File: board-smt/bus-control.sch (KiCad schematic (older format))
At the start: 75 parts, among them Q301 Dual_NMOS, Q302 Dual_NMOS, Q303 Dual_NMOS, Q304 Dual_NMOS, Q305 Dual_NMOS, Q306 Dual_NMOS, Q307 Dual_NMOS, U201 CMP401, U204 CMP401, U205 CMP401, U301 CMP401, U302 CMP401, U303 CMP401, U304 CMP401, U305 CMP401

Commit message: Added some voltage regulators.
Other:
- note added: "Need to split the 1.5V reference bus\ninto two halves with separate regulators."
- note removed: "Need to split the 1.5V bus into two\nhalves with separate regulators."
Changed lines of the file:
@@
 	6200 5150 6200 5100
 Text Notes 5350 5900 0    60   ~ 0
-Need to split the 1.5V bus into two\nhalves with separate regulators.
+Need to split the 1.5V reference bus\ninto two halves with separate regulators.
 Wire Wire Line
 	2650 1200 2650 1250

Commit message: Worked on the board layout for the bus receivers.
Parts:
- renumbered Q307 to Q308, U302 to U205, U205 to U302
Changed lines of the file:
@@
 $EndComp
 $Comp
-L CMP401 U205
-U 2 1 58C6BC47
+L CMP401 U302
+U 1 1 58C6BC47
 P 8950 3900
-F 0 "U205" H 9450 4000 60  0000 C CNN
+F 0 "U302" H 9450 4000 60  0000 C CNN
 F 1 "CMP401" H 9550 3700 60  0000 C CNN
 F 2 "Housings_SOIC:SOIC-16_3.9x9.9mm_Pitch1.27mm" H 8950 3900 60  0001 C CNN
 F 3 "" H 8950 3900 60  0001 C CNN
-	2    8950 3900
+	1    8950 3900
 	1    0    0    -1
 $EndComp
@@
 	5450 2150 5350 2150
 $Comp
-L Dual_NMOS Q307
-U 2 1 58C6D401
+L Dual_NMOS Q308
+U 1 1 58C6D401
 P 5500 3200
-F 0 "Q307" H 5450 3100 50  0000 R CNN
+F 0 "Q308" H 5450 3100 50  0000 R CNN
 F 1 "Dual_NMOS" H 5500 3000 50  0000 R CNN
 F 2 "TO_SOT_Packages_SMD:SOT-23-6" H 5700 3300 29  0001 C CNN
 F 3 "" H 5500 3200 60  0000 C CNN
-	2    5500 3200
+	1    5500 3200
 	1    0    0    -1
 $EndComp
@@
 $EndComp
 $Comp
-L CMP401 U302
-U 1 1 58C6D435
+L CMP401 U205
+U 3 1 58C6D435
 P 6000 3150
-F 0 "U302" H 6500 3250 60  0000 C CNN
+F 0 "U205" H 6500 3250 60  0000 C CNN
 F 1 "CMP401" H 6600 2950 60  0000 C CNN
 F 2 "Housings_SOIC:SOIC-16_3.9x9.9mm_Pitch1.27mm" H 6000 3150 60  0001 C CNN
 F 3 "" H 6000 3150 60  0001 C CNN
-	1    6000 3150
+	3    6000 3150
 	1    0    0    -1
 $EndComp
@@
 $Comp
 L CMP401 U205
-U 3 1 58C6FE61
+U 2 1 58C6FE61
 P 1950 2700
 F 0 "U205" H 2450 2800 60  0000 C CNN
@@
 F 2 "Housings_SOIC:SOIC-16_3.9x9.9mm_Pitch1.27mm" H 1950 2700 60  0001 C CNN
 F 3 "" H 1950 2700 60  0001 C CNN
-	3    1950 2700
-	1    0    0    -1
-$EndComp
+	2    1950 2700
+	1    0    0    -1
+$EndComp

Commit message: Moved comparator power connections to separate symbols.
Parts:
- removed R360: 5kΩ, Resistors_SMD:R_0603, symbol R
- R335, R336: value R -> 20kΩ
- R347, R348: value R -> 340kΩ
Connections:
- net labels added: +1V5_ref
- net labels removed: +3V3
- wire segments 231 -> 213
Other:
- note added: "If split the 1.5V reference,\nuse two 10k resistors."
- note removed: "Need to split the 1.5V reference bus\ninto two halves with separate regulators."

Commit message: Little fixups
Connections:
- wire segments 213 -> 156

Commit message: Updated to KiCad v5
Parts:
- Q301, Q302, Q303, Q304, Q305, Q306, Q307, Q308: symbol Dual_NMOS -> myLib:Dual_NMOS
- R301, R302, R303, R304, R305, R306, R307, R308, R309, R310, R311, R312, R313, R314, R315, R316, R317, R318, R319, R320, R321, R322, R323, R324, R325, R326, R327, R328, R329, R330, R331, R332, R333, R334, R335, R336, R337, R338, R339, R340, R341, R342, R343, R344, R345, R346, R347, R348, R349, R350, R351, R352, R353, R354, R355, R356, R357, R358, R359: symbol R -> device:R
- U201, U204, U205, U301, U302, U303, U304, U305: symbol CMP401 -> myLib:CMP401
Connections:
- wire segments 156 -> 212

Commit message: Updated to KiCad v5
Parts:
- R301, R302, R303, R304, R305, R306, R307, R308, R309, R310, R311, R312, R313, R314, R315, R316, R317, R318, R319, R320, R321, R322, R323, R324, R325, R326, R327, R328, R329, R330, R331, R332, R333, R334, R335, R336, R337, R338, R339, R340, R341, R342, R343, R344, R345, R346, R347, R348, R349, R350, R351, R352, R353, R354, R355, R356, R357, R358, R359: symbol device:R -> qsic-rescue:R-device
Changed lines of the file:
@@
 EESchema Schematic File Version 4
 LIBS:qsic-cache
-EELAYER 26 0
+EELAYER 30 0
 EELAYER END
 $Descr A 11000 8500
 encoding utf-8
-Sheet 2 6
+Sheet 2 7
 Title "Bus Control Transceivers"
 Date "2017-10-31"
@@
 $EndComp
 $Comp
-L device:R R323
+L qsic-rescue:R-device R323
 U 1 1 5885877B
 P 8050 1100
@@
 $EndComp
 $Comp
-L device:R R335
+L qsic-rescue:R-device R335
 U 1 1 58858792
 P 8900 1350
@@
 $EndComp
 $Comp
-L device:R R347
+L qsic-rescue:R-device R347
 U 1 1 58858799
 P 9100 1200
@@
 $EndComp
 $Comp
-L device:R R317
+L qsic-rescue:R-device R317
 U 1 1 58859CC4
 P 3650 5500
@@
 $EndComp
 $Comp
-L device:R R318
+L qsic-rescue:R-device R318
 U 1 1 58859CD5
 P 3650 6950
@@
 $EndComp
 $Comp
-L device:R R302
+L qsic-rescue:R-device R302
 U 1 1 58859D09
 P 1500 5300
@@
 $EndComp
 $Comp
-L device:R R301
+L qsic-rescue:R-device R301
 U 1 1 58859D11
 P 1500 4900
@@
 $EndComp
 $Comp
-L device:R R319
+L qsic-rescue:R-device R319
 U 1 1 58859D26
 P 4300 5100
@@
 $EndComp
 $Comp
-L device:R R320
+L qsic-rescue:R-device R320
 U 1 1 58859D2D
 P 4300 5500
@@
 $EndComp
 $Comp
-L device:R R304
+L qsic-rescue:R-device R304
 U 1 1 58859D48
 P 1500 6750
@@
 $EndComp
 $Comp
-L device:R R303
+L qsic-rescue:R-device R303
 U 1 1 58859D55
 P 1500 6350
@@
 $EndComp
 $Comp
-L device:R R321
+L qsic-rescue:R-device R321
 U 1 1 58859D5E
 P 4300 6550
@@
 $EndComp
 $Comp
-L device:R R322
+L qsic-rescue:R-device R322
 U 1 1 58859D6B
 P 4300 6950
@@
 $EndComp
 $Comp
-L device:R R305
+L qsic-rescue:R-device R305
 U 1 1 58859DCE
 P 1500 1000
@@
 $EndComp
 $Comp
-L device:R R311
+L qsic-rescue:R-device R311
 U 1 1 58859DD5
 P 2050 1000
@@
 $EndComp
 $Comp
-L device:R R306
+L qsic-rescue:R-device R306
 U 1 1 58859DF7
 P 1550 1750
@@
 $EndComp
 $Comp
-L device:R R312
+L qsic-rescue:R-device R312
 U 1 1 58859E7E
 P 2100 1750
@@
 	1650 2050 1750 2050
 $Comp
-L device:R R359
+L qsic-rescue:R-device R359
 U 1 1 58865DB5
 P 5900 5300
@@
 $EndComp
 $Comp
-L device:R R324
+L qsic-rescue:R-device R324
 U 1 1 58C69285
 P 8050 1800
@@
 $EndComp
 $Comp
-L device:R R336
+L qsic-rescue:R-device R336
 U 1 1 58C69298
 P 8900 2050
@@
 $EndComp
 $Comp
-L device:R R348
+L qsic-rescue:R-device R348
 U 1 1 58C6929F
 P 9100 1900
@@
 $EndComp
 $Comp
-L device:R R325
+L qsic-rescue:R-device R325
 U 1 1 58C6B57E
 P 8050 2550
@@
 $EndComp
 $Comp
-L device:R R337
+L qsic-rescue:R-device R337
 U 1 1 58C6B591
 P 8900 2800
@@
 $EndComp
 $Comp
-L device:R R349
+L qsic-rescue:R-device R349
 U 1 1 58C6B598
 P 9100 2650
@@
 $EndComp
 $Comp
-L device:R R326
+L qsic-rescue:R-device R326
 U 1 1 58C6B9FE
 P 8050 3250
@@
 $EndComp
 $Comp
-L device:R R338
+L qsic-rescue:R-device R338
 U 1 1 58C6BA11
 P 8900 3500
@@
 $EndComp
 $Comp
-L device:R R350
+L qsic-rescue:R-device R350
 U 1 1 58C6BA18
 P 9100 3350
@@
 $EndComp
 $Comp
-L device:R R327
+L qsic-rescue:R-device R327
 U 1 1 58C6BC1A
 P 8050 3950
@@
 $EndComp
 $Comp
-L device:R R339
+L qsic-rescue:R-device R339
 U 1 1 58C6BC2D
 P 8900 4200
@@
 $EndComp
 $Comp
-L device:R R351
+L qsic-rescue:R-device R351
 U 1 1 58C6BC34
 P 9100 4050
@@
 $EndComp
 $Comp
-L device:R R328
+L qsic-rescue:R-device R328
 U 1 1 58C6C09D
 P 8050 4650
@@
 $EndComp
 $Comp
-L device:R R340
+L qsic-rescue:R-device R340
 U 1 1 58C6C0B0
 P 8900 4900
@@
 $EndComp
 $Comp
-L device:R R352
+L qsic-rescue:R-device R352
 U 1 1 58C6C0B7
 P 9100 4750
@@
 $EndComp
 $Comp
-L device:R R329
+L qsic-rescue:R-device R329
 U 1 1 58C6C381
 P 8050 5350
@@
 $EndComp
 $Comp
-L device:R R341
+L qsic-rescue:R-device R341
 U 1 1 58C6C394
 P 8900 5600
@@
 $EndComp
 $Comp
-L device:R R353
+L qsic-rescue:R-device R353
 U 1 1 58C6C39B
 P 9100 5450
@@
 $EndComp
 $Comp
-L device:R R330
+L qsic-rescue:R-device R330
 U 1 1 58C6C90E
 P 8050 6050
@@
 $EndComp
 $Comp
-L device:R R342
+L qsic-rescue:R-device R342
 U 1 1 58C6C921
 P 8900 6300
@@
 $EndComp
 $Comp
-L device:R R354
+L qsic-rescue:R-device R354
 U 1 1 58C6C928
 P 9100 6150
@@
 $EndComp
 $Comp
-L device:R R331
+L qsic-rescue:R-device R331
 U 1 1 58C6CADA
 P 4600 1200
@@
 $EndComp
 $Comp
-L device:R R343
+L qsic-rescue:R-device R343
 U 1 1 58C6CAED
 P 5450 1450
@@
 $EndComp
 $Comp
-L device:R R355
+L qsic-rescue:R-device R355
 U 1 1 58C6CAF4
 P 5650 1300
@@
 $EndComp
 $Comp
-L device:R R332
+L qsic-rescue:R-device R332
 U 1 1 58C6CDF5
 P 4600 1900
@@
 $EndComp
 $Comp
-L device:R R344
+L qsic-rescue:R-device R344
 U 1 1 58C6CE08
 P 5450 2150
@@
 $EndComp
 $Comp
-L device:R R356
+L qsic-rescue:R-device R356
 U 1 1 58C6CE0F
 P 5650 2000
@@
 $EndComp
 $Comp
-L device:R R333
+L qsic-rescue:R-device R333
 U 1 1 58C6D0CF
 P 4600 2650
@@
 $EndComp
 $Comp
-L device:R R345
+L qsic-rescue:R-device R345
 U 1 1 58C6D0E2
 P 5450 2900
@@
 $EndComp
 $Comp
-L device:R R357
+L qsic-rescue:R-device R357
 U 1 1 58C6D0E9
 P 5650 2750
@@
 $EndComp
 $Comp
-L device:R R334
+L qsic-rescue:R-device R334
 U 1 1 58C6D408
 P 4600 3400
@@
 $EndComp
 $Comp
-L device:R R346
+L qsic-rescue:R-device R346
 U 1 1 58C6D41B
 P 5450 3650
@@
 $EndComp
 $Comp
-L device:R R358
+L qsic-rescue:R-device R358
 U 1 1 58C6D422
 P 5650 3500
@@
 	4400 3400 4450 3400
 $Comp
-L device:R R307
+L qsic-rescue:R-device R307
 U 1 1 58C6FE47
 P 1550 2500
@@
 $EndComp
 $Comp
-L device:R R313
+L qsic-rescue:R-device R313
 U 1 1 58C6FE4E
 P 2100 2500
@@
 	1650 2800 1750 2800
 $Comp
-L device:R R308
+L qsic-rescue:R-device R308
 U 1 1 58C708D6
 P 1550 3300
@@
 $EndComp
 $Comp
-L device:R R314
+L qsic-rescue:R-device R314
 U 1 1 58C708DD
 P 2100 3300
@@
 $EndComp
 $Comp
-L device:R R309
+L qsic-rescue:R-device R309
 U 1 1 58C71611
 P 1900 4800
@@
 $EndComp
 $Comp
-L device:R R315
+L qsic-rescue:R-device R315
 U 1 1 58C71618
 P 2450 4800
@@
 $EndComp
 $Comp
-L device:R R310
+L qsic-rescue:R-device R310
 U 1 1 58C73CFA
 P 1900 6250
@@
 $EndComp
 $Comp
-L device:R R316
+L qsic-rescue:R-device R316
 U 1 1 58C73D01
 P 2450 6250
@@
 Wire Wire Line
 	8750 1200 8750 1350
+$Sheet
+S 5025 4100 825  425
+U 5CBC325F
+F0 "Sheet5CBC325E" 60
+F1 "xcvr.sch" 60
+F2 "Trans" I L 5025 4400 60
+F3 "Bus" B L 5025 4200 60
+F4 "Rec" O R 5850 4400 60
+F5 "1V5_ref" I R 5850 4200 60
+$EndSheet
+$Comp
+L myLib:+1V5_ref #PWR?
+U 1 1 5CBC702F
+P 5950 4200
+F 0 "#PWR?" H 5950 4050 50  0001 C CNN
+F 1 "+1V5_ref" V 5950 4500 50  0000 C CNN
+F 2 "" H 5950 4200 50  0001 C CNN
+F 3 "" H 5950 4200 50  0001 C CNN
+	1    5950 4200
+	0    1    1    0
+$EndComp
+Text HLabel 5950 4400 2    60   Output ~ 0
+RIRQ7
+Text HLabel 4950 4400 0    60   Input ~ 0
+TIRQ7
+Text HLabel 4950 4200 0    60   BiDi ~ 0
+BIRQ7
+Wire Wire Line
+	4950 4200 5025 4200
+Wire Wire Line
+	4950 4400 5025 4400
+Wire Wire Line
+	5850 4200 5950 4200
+Wire Wire Line
+	5850 4400 5950 4400
 $EndSCHEMATC

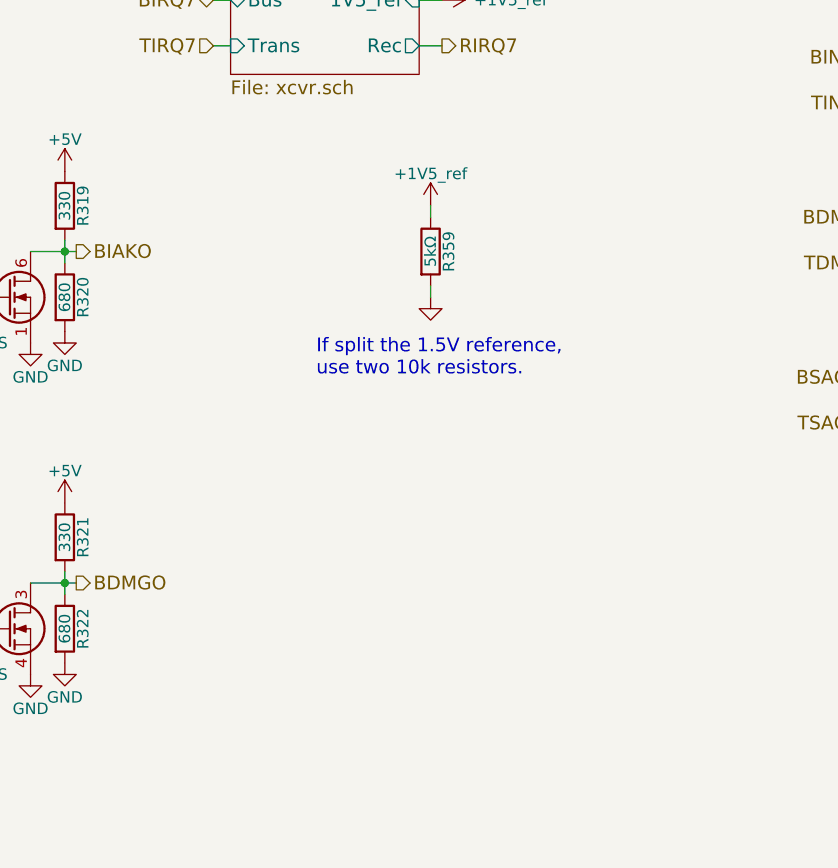
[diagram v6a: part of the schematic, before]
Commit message: These are all old changes in directories that are now historical.
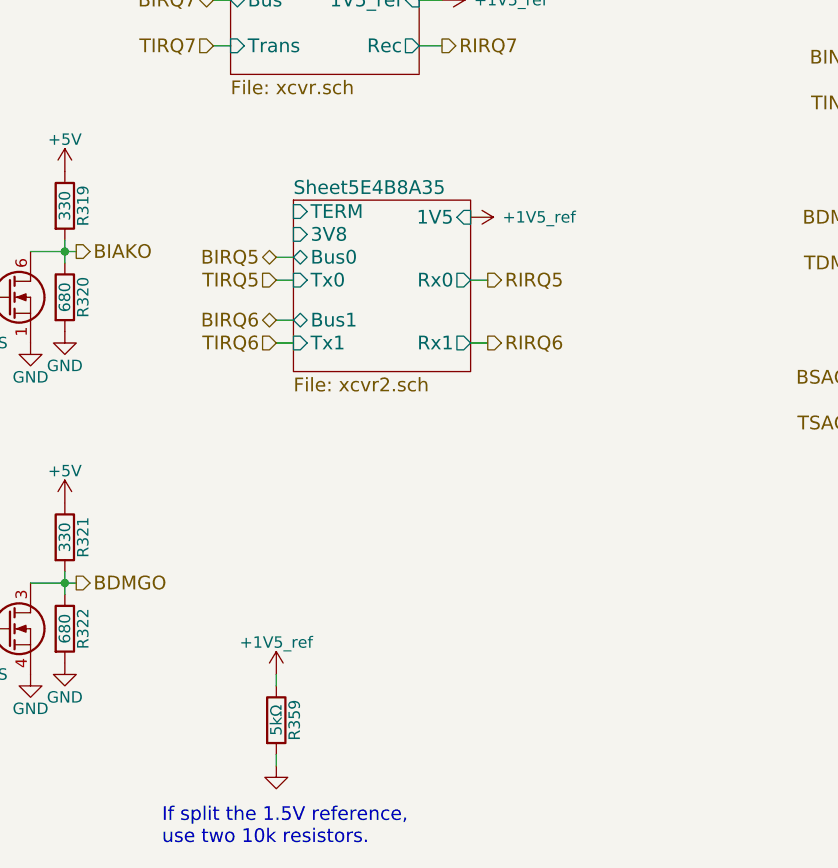
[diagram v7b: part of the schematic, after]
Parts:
- R301, R302, R303, R304, R305, R306, R307, R308, R309, R310, R311, R312, R313, R314, R315, R316, R317, R318, R319, R320, R321, R322, R323, R324, R325, R326, R327, R328, R329, R330, R331, R332, R333, R334, R335, R336, R337, R338, R339, R340, R341, R342, R343, R344, R345, R346, R347, R348, R349, R350, R351, R352, R353, R354, R355, R356, R357, R358, R359: footprint Resistors_SMD:R_0603 -> Resistor_SMD:R_0603_1608Metric
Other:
- moved on the sheet: R359
